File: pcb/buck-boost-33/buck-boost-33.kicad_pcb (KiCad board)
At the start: 2 copper layers, 23.5 x 17.5 mm, 14 parts, among them IC1 TP4056, J1 BATT, J2 buck-boost-conn, J3 PWR, U1 TPS63031DSKT

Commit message: rework with new footprints
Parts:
- C1: moved to F.Cu
- L1: footprint coil:Murata 1266AS-H-1R5N=P2 -> coil:Murata_1266AS-H-1R5N=P2
- moved C5 5.86 mm to (94.0, 85.2), turned to 180 degrees
- moved J2 5.76 mm to (102.8, 79.8)
- moved C1 5.13 mm to (96.8, 80.5), turned to 270 degrees
- moved IC1 4.26 mm to (102.2, 80.2)
- moved C6 3.88 mm to (107.5, 89.2)
- moved C4 3.82 mm to (105.2, 89.2)
- moved C2 3.76 mm to (99.2, 89.2)
- moved L1 3.76 mm to (102.2, 85.8)
- moved C3 3.29 mm to (102.5, 92.2)
- moved J3 3.26 mm to (91.2, 82.2), turned to 180 degrees
- moved U1 3.26 mm to (102.2, 89.2)
- moved J1 3.04 mm to (96.0, 89.0)
- moved R2 0.56 mm to (94.2, 76.0), turned to 180 degrees
- moved R1 0.50 mm to (94.5, 80.5), turned to 270 degrees
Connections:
- net Net-(C4-Pad2) renamed /3.3V
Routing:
- net BATT: track 22.7 -> 45.3 mm, vias 1 -> 2
- net +5V: track 3.16 -> 15.5 mm
- net GND: track 79.5 -> 67.4 mm, vias 5 -> 2
- net Net-(C1-Pad1): track 21.4 -> 16.9 mm, vias 3 -> 4
- net CHRG: track 6.30 -> 9.84 mm
- net Net-(IC1-Pad2): track 2.74 -> 6.02 mm
- net STDBY: track 8.39 -> 10.2 mm
- net /3.3V: track 21.5 -> 22.7 mm
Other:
- board size 23.5 x 17.5 mm -> 20 x 20 mm

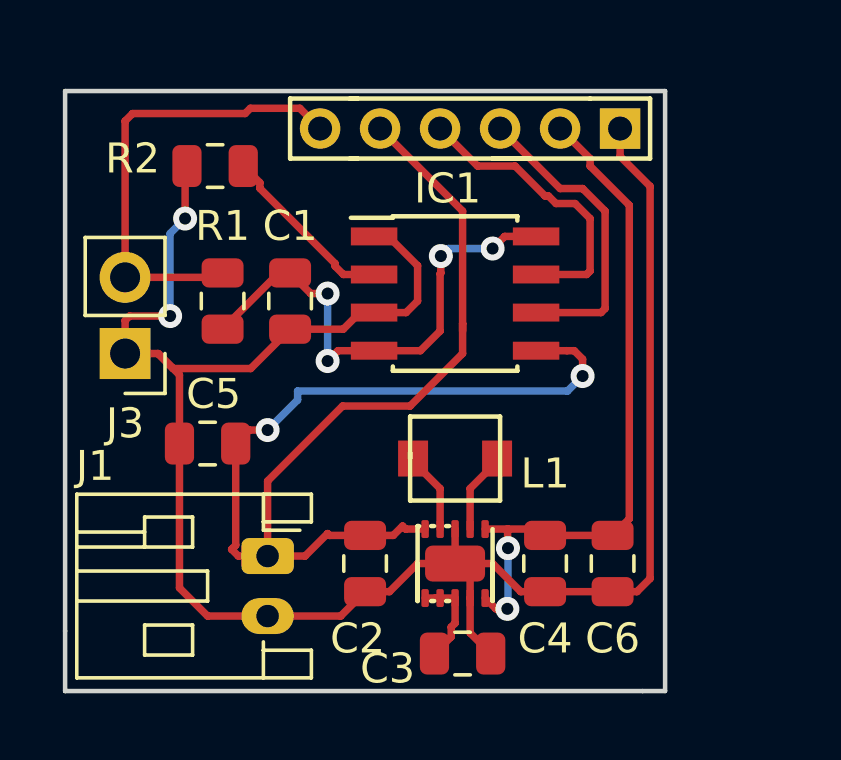
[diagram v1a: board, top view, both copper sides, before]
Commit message: add LCSC part numbers, use another coil
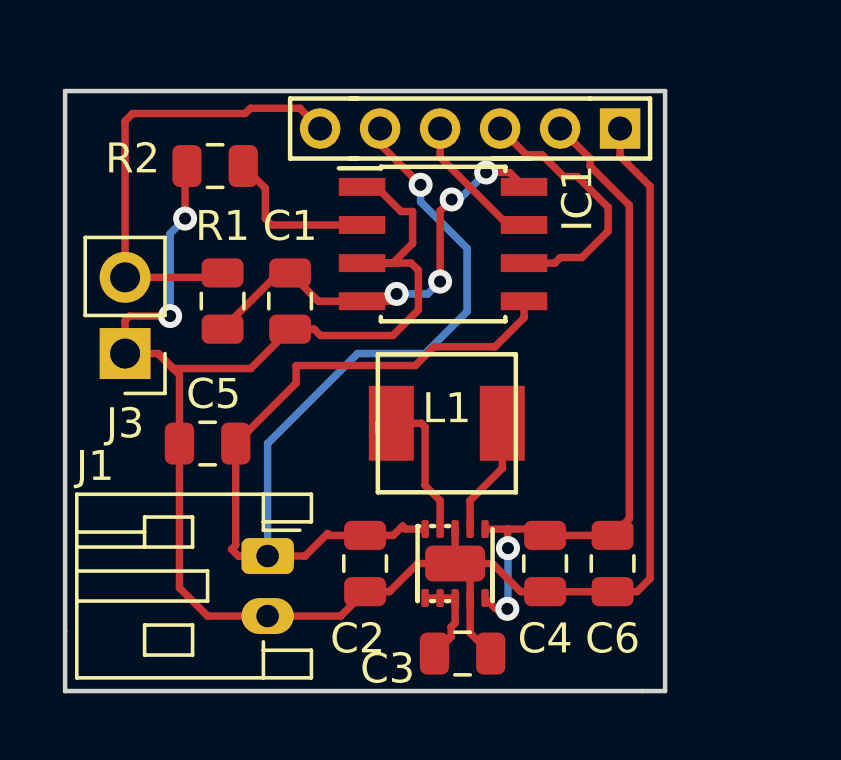
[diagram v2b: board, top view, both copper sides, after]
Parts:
- L1: footprint coil:Murata_1266AS-H-1R5N=P2 -> coil:CoilMX-MS0420
- moved IC1 1.70 mm to (101.8, 78.6)
- moved L1 1.21 mm to (102.0, 84.6), turned to 180 degrees
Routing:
- net GND: track 67.4 -> 72.8 mm
- net CHRG: track 9.84 -> 4.69 mm
- net Net-(C1-Pad1): track 16.9 -> 14.6 mm
- net BATT: track 45.3 -> 43.1 mm, vias 2 -> 1
- net Net-(L1-Pad1): track 2.92 -> 4.78 mm
- net STDBY: track 10.2 -> 8.73 mm
- net Net-(L1-Pad2): track 2.72 -> 3.97 mm
- net Net-(IC1-Pad2): track 6.02 -> 5.37 mm

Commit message: update
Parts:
- moved L1 0.40 mm to (102.0, 85.0)
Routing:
- net Net-(L1-Pad1): track 4.78 -> 3.80 mm
- added copper zone on F.Cu, net /3.3V
- added copper zone on F.Cu, net BATT
- added copper zone on B.Cu, net GND
- added copper zone on F.Cu, net GND
- added copper zone on F.Cu, net Net-(L1-Pad1)
- added copper zone on F.Cu, net Net-(L1-Pad2)
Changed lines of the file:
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@@
     (thickness 1.6)
     (drawings 6)
-    (tracks 157)
+    (tracks 155)
     (zones 0)
     (modules 14)
@@
       (creategerberjobfile false)
       (excludeedgelayer true)
-      (linewidth 0.100000)
+      (linewidth 0.150000)
       (plotframeref false)
       (viasonmask false)
@@
       (drillshape 0)
       (scaleselection 1)
-      (outputdirectory "/tmp/"))
+      (outputdirectory "/tmp/buckboost/"))
   )
   (net 0 "")
@@
   )
   (module coil:CoilMX-MS0420 (layer F.Cu)
-    (at 101.975 84.575 180)
+    (at 101.975 84.975 180)
     (descr https://datasheet.lcsc.com/szlcsc/1912111437_COILMX-MS0420-1R5M_C380153.pdf)
+    (attr smd)
     (fp_text reference L1 (at 0 0.5 180) (layer F.SilkS)
       (effects (font (size 1 1) (thickness 0.15)))
@@
       (effects (font (size 1 1) (thickness 0.15)))
     )
-    (fp_line (start 2.3 2.3) (end 2.3 -0.3) (layer F.SilkS) (width 0.15))
-    (fp_line (start -2.3 2.3) (end 2.3 2.3) (layer F.SilkS) (width 0.15))
-    (fp_line (start -2.3 -2.3) (end -2.3 2.3) (layer F.SilkS) (width 0.15))
-    (fp_line (start 2.3 -2.3) (end -2.3 -2.3) (layer F.SilkS) (width 0.15))
-    (fp_line (start 2.3 0) (end 2.3 -2.3) (layer F.SilkS) (width 0.15))
+    (fp_line (start 2.3 0) (end 2.3 -2.1) (layer F.SilkS) (width 0.15))
+    (fp_line (start -2.3 -2.1) (end -2.3 2.1) (layer F.SilkS) (width 0.15))
+    (fp_line (start 2.3 2.1) (end 2.3 -0.3) (layer F.SilkS) (width 0.15))
+    (fp_line (start 0 2.1) (end 2.3 2.1) (layer F.SilkS) (width 0.15))
+    (fp_line (start 2.3 2.1) (end -2.3 2.1) (layer F.SilkS) (width 0.15))
+    (fp_line (start 0 -2.1) (end 2.3 -2.1) (layer F.SilkS) (width 0.15))
+    (fp_line (start 2.3 -2.1) (end -2.3 -2.1) (layer F.SilkS) (width 0.15))
+    (pad 1 smd rect (at 1.85 0 180) (size 1.5 2.5) (layers F.Cu F.Paste F.Mask)
+      (net 4 "Net-(L1-Pad1)"))
     (pad 2 smd rect (at -1.85 0 180) (size 1.5 2.5) (layers F.Cu F.Paste F.Mask)
       (net 5 "Net-(L1-Pad2)"))
-    (pad 1 smd rect (at 1.85 0 180) (size 1.5 2.5) (layers F.Cu F.Paste F.Mask)
-      (net 4 "Net-(L1-Pad1)"))
   )
   (module Connector_PinHeader_2.54mm:PinHeader_1x02_P2.54mm_Vertical (layer F.Cu)
@@
   (segment (start 96 85.25) (end 96 89) (width 0.25) (layer B.Cu) (net 3))
   (segment (start 99 82.25) (end 96 85.25) (width 0.25) (layer B.Cu) (net 3))
-  (segment (start 101.125 84.575) (end 101.25 84.7) (width 0.25) (layer F.Cu) (net 4))
-  (segment (start 100.125 84.575) (end 101.125 84.575) (width 0.25) (layer F.Cu) (net 4))
-  (segment (start 101.25 84.7) (end 101.25 86.65) (width 0.25) (layer F.Cu) (net 4))
-  (segment (start 101.75 87.15) (end 101.75 88.1) (width 0.25) (layer F.Cu) (net 4))
-  (segment (start 101.25 86.65) (end 101.75 87.15) (width 0.25) (layer F.Cu) (net 4))
-  (segment (start 102.75 87.15) (end 102.75 88.1) (width 0.25) (layer F.Cu) (net 5))
-  (segment (start 103.825 86.075) (end 102.75 87.15) (width 0.25) (layer F.Cu) (net 5))
-  (segment (start 103.825 84.575) (end 103.825 86.075) (width 0.25) (layer F.Cu) (net 5))
+  (segment (start 100.125 85.475) (end 100.125 84.975) (width 0.25) (layer F.Cu) (net 4))
+  (segment (start 101.75 87.1) (end 100.125 85.475) (width 0.25) (layer F.Cu) (net 4))
+  (segment (start 101.75 88.1) (end 101.75 87.1) (width 0.25) (layer F.Cu) (net 4))
+  (segment (start 103.825 85.475) (end 103.825 84.975) (width 0.25) (layer F.Cu) (net 5))
+  (segment (start 102.75 86.55) (end 103.825 85.475) (width 0.25) (layer F.Cu) (net 5))
+  (segment (start 102.75 88.1) (end 102.75 86.55) (width 0.25) (layer F.Cu) (net 5))
   (segment (start 104.625 75.625) (end 103.75 74.75) (width 0.25) (layer F.Cu) (net 6))
   (segment (start 105.144998 75.625) (end 104.625 75.625) (width 0.25) (layer F.Cu) (net 6))
@@
   (segment (start 103.609781 90.759781) (end 103.25 90.4) (width 0.25) (layer F.Cu) (net 11))
   (segment (start 103.992393 90.759781) (end 103.609781 90.759781) (width 0.25) (layer F.Cu) (net 11))
+  (zone (net 4) (net_name "Net-(L1-Pad1)") (layer F.Cu) (hatch edge 0.508)
+    (connect_pads (clearance 0.508))
+    (min_thickness 0.254)
+    (fill yes (arc_segments 16) (thermal_gap 0.508) (thermal_bridge_width 0.508))
+    (polygon
+      (pts
+        (xy 101.9 87.625) (xy 101.825 86) (xy 100.9 85.225) (xy 99.25 85.225) (xy 99.275 86.525)
+        (xy 100.725 86.525) (xy 101.4 87) (xy 101.6 87.475) (xy 101.6 87.825)
+      )
+    )
+  )
+  (zone (net 5) (net_name "Net-(L1-Pad2)") (layer F.Cu) (hatch edge 0.508)
+    (connect_pads (clearance 0.508))
+    (min_thickness 0.254)
+    (fill yes (arc_segments 16) (thermal_gap 0.508) (thermal_bridge_width 0.508))
+    (polygon
+      (pts
+        (xy 102.625 87.725) (xy 102.6 85.95) (xy 104.525 85.95) (xy 104.525 86.45) (xy 103.775 86.675)
+        (xy 103.3 86.8) (xy 102.975 86.95) (xy 102.925 87.775)
+      )
+    )
+  )
+  (zone (net 3) (net_name BATT) (layer F.Cu) (hatch edge 0.508)
+    (connect_pads (clearance 0.508))
+    (min_thickness 0.254)
+    (fill yes (arc_segments 16) (thermal_gap 0.508) (thermal_bridge_width 0.508))
+    (polygon
+      (pts
+        (xy 95.1 87.675) (xy 97.775 87.475) (xy 100.325 87.525) (xy 101.375 87.75) (xy 101.4 88.425)
+        (xy 100.575 88.425) (xy 100.15 88.75) (xy 99.9 89) (xy 98.75 89) (xy 97.3 89.2)
+        (xy 96.95 89.75) (xy 95.025 89.775)
+      )
+    )
+  )
+  (zone (net 1) (net_name GND) (layer F.Cu) (hatch edge 0.508)
+    (connect_pads (clearance 0.508))
+    (min_thickness 0.254)
+    (fill yes (arc_segments 16) (thermal_gap 0.508) (thermal_bridge_width 0.508))
+    (polygon
+      (pts
+        (xy 96.025 90.175) (xy 97.175 90.075) (xy 97.775 89.85) (xy 99.1 89.575) (xy 100.325 89.35)
+        (xy 101.35 89.05) (xy 101.325 89.575) (xy 100.85 89.75) (xy 100.55 90.225) (xy 100.225 90.725)
+        (xy 99.475 91.025) (xy 95.6 91.925) (xy 94.8 91.85) (xy 94.8 90.35)
+      )
+    )
+  )
+  (zone (net 1) (net_name GND) (layer F.Cu) (hatch edge 0.508)
+    (connect_pads (clearance 0.508))
+    (min_thickness 0.254)
+    (fill yes (arc_segments 16) (thermal_gap 0.508) (thermal_bridge_width 0.508))
+    (polygon
+      (pts
+        (xy 103.275 89.125) (xy 104.25 89.45) (xy 109.075 89.25) (xy 109.125 91.1) (xy 104.75 91.1)
+        (xy 103.65 90.1)
+      )
+    )
+  )
+  (zone (net 11) (net_name /3.3V) (layer F.Cu) (hatch edge 0.508)
+    (connect_pads (clearance 0.508))
+    (min_thickness 0.254)
+    (fill yes (arc_segments 16) (thermal_gap 0.508) (thermal_bridge_width 0.508))
+    (polygon
+      (pts
+        (xy 103.1 87.375) (xy 107.8 87.325) (xy 107.825 86.65) (xy 108.375 86.725) (xy 108.375 87.6)
+        (xy 108.45 88.9) (xy 106.675 89.025) (xy 103.725 88.8) (xy 103.15 88.35)
+      )
+    )
+  )
+  (zone (net 1) (net_name GND) (layer B.Cu) (hatch edge 0.508)
+    (connect_pads (clearance 0.508))
+    (min_thickness 0.254)
+    (fill yes (arc_segments 16) (thermal_gap 0.508) (thermal_bridge_width 0.508))
+    (polygon
+      (pts
+        (xy 89.45 73.65) (xy 106.85 73.75) (xy 106.875 82.675) (xy 96.375 82.85) (xy 96.225 86.725)
+        (xy 89.475 86.925)
+      )
+    )
+  )
 )

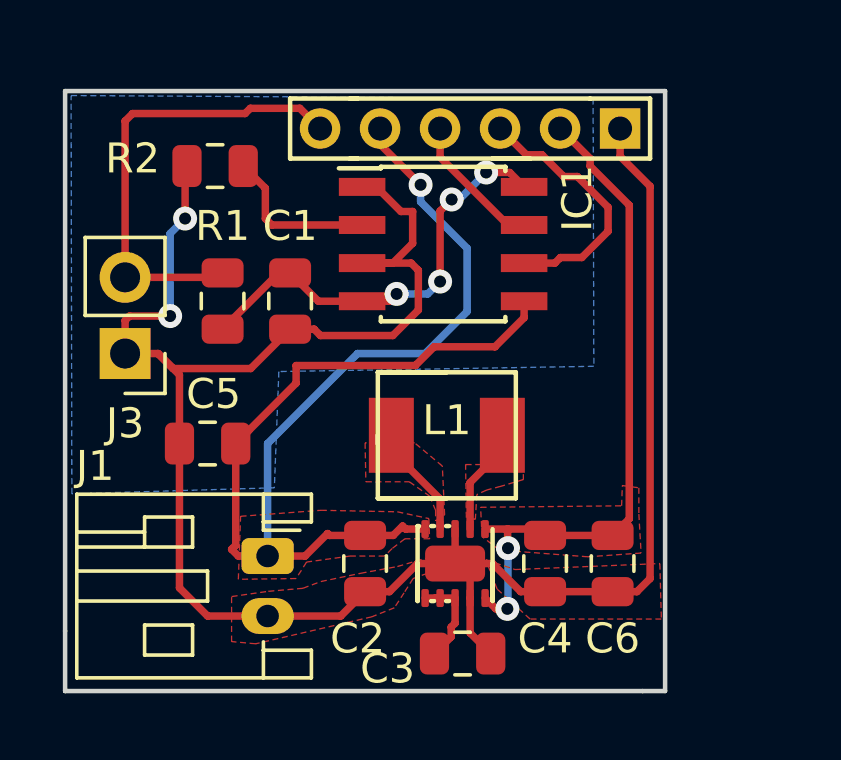
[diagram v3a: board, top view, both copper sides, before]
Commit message: back to marata inductor; smaller pcb
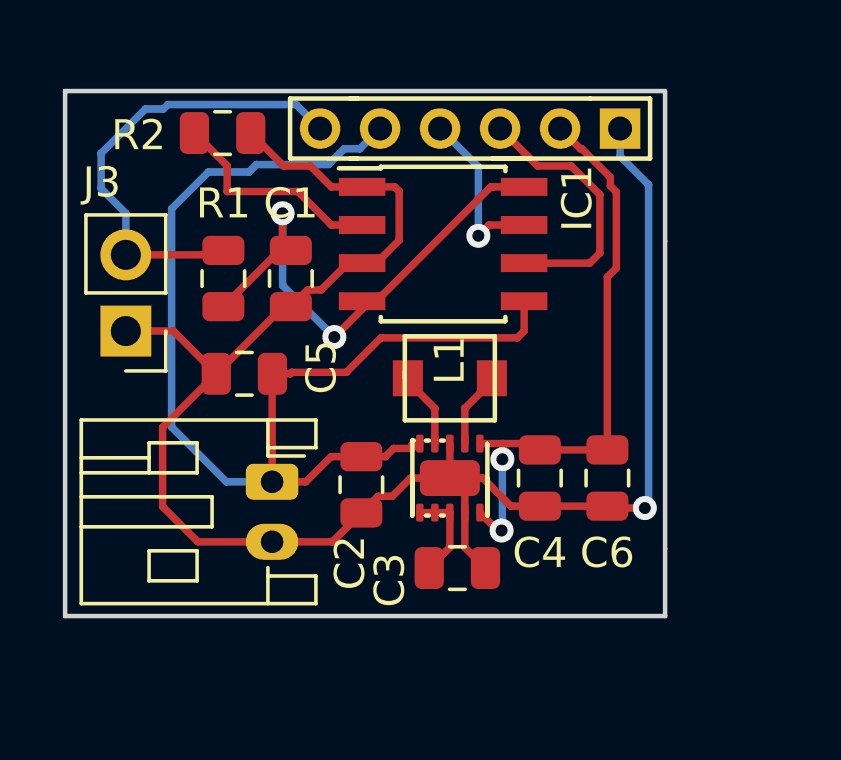
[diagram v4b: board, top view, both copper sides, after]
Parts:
- L1: footprint coil:CoilMX-MS0420 -> coil:Murata_1266AS-H-1R5N=P2
- moved C3 2.86 mm to (102.3, 89.4)
- moved C4 2.86 mm to (105.1, 86.4)
- moved C6 2.86 mm to (107.3, 86.4)
- moved U1 2.86 mm to (102.1, 86.4)
- moved C5 2.63 mm to (95.2, 82.9)
- moved C2 2.63 mm to (99.1, 86.6)
- moved J1 2.48 mm to (96.2, 86.5)
- moved L1 1.90 mm to (102.1, 83.1), turned to 90 degrees
- moved R2 1.13 mm to (94.5, 74.9), turned to 0 degrees
- moved C1 0.75 mm to (96.8, 79.8)
- moved J3 0.75 mm to (91.3, 81.5)
- moved R1 0.75 mm to (94.5, 79.8)
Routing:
- net GND: track 72.8 -> 59.7 mm, vias 2 -> 1
- net BATT: track 43.1 -> 38.5 mm, vias 1 -> 0
- net Net-(C1-Pad1): track 14.6 -> 17.8 mm, vias 4 -> 2
- net /3.3V: track 22.7 -> 19.9 mm
- net Net-(IC1-Pad2): track 5.37 -> 7.36 mm
- net Net-(L1-Pad1): track 3.80 -> 2.55 mm
- net CHRG: track 4.69 -> 5.78 mm, vias 0 -> 1
- net Net-(L1-Pad2): track 3.57 -> 2.55 mm
- removed copper zone on F.Cu, net /3.3V
- removed copper zone on F.Cu, net BATT
- removed copper zone on B.Cu, net GND
- removed copper zone on F.Cu, net GND
- removed copper zone on F.Cu, net Net-(L1-Pad1)
- removed copper zone on F.Cu, net Net-(L1-Pad2)
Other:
- board size 20 x 20 mm -> 20 x 17.5 mm

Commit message: update
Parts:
- added P-G: 0, Resistor_SMD:R_0805_2012Metric, B.Cu at (93.2, 89.0)
- added P-V: 0, Resistor_SMD:R_0805_2012Metric, B.Cu at (91.0, 89.0)
- moved C2 0.88 mm to (99.2, 85.8)
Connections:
- U1 pad 6: Net-(C3-Pad2) -> BATT
- U1 pad 7: Net-(C3-Pad2) -> Net-(R3-Pad1)
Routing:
- net Net-(R3-Pad1): track 0.00 -> 11.9 mm, vias 0 -> 1
- net BATT: track 38.5 -> 49.8 mm, vias 0 -> 1
- net /3.3V: track 19.9 -> 23.0 mm
- net GND: track 59.7 -> 62.1 mm, vias 1 -> 2
- net Net-(C3-Pad2): track 3.13 -> 2.13 mm
- added copper zone on F.Cu, net /3.3V
- added copper zone on F.Cu, net BATT
- added copper zone on B.Cu, net GND
- added copper zone on F.Cu, net GND
- added copper zone on F.Cu, net Net-(L1-Pad1)
- added copper zone on F.Cu, net Net-(L1-Pad2)
